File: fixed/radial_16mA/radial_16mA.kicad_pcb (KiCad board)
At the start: 2 copper layers, 25.4 x 20 mm, 18 parts, among them J1 Conn_01x04, J2 Conn_01x04, M1 MountingHole_2.5mm_Pad, M2 MountingHole_2.5mm_Pad, M3 MountingHole_2.5mm_Pad, M4 MountingHole_2.5mm_Pad, Q1 MMBT5551L, U1 TPS61222DCK, U2 LMV321

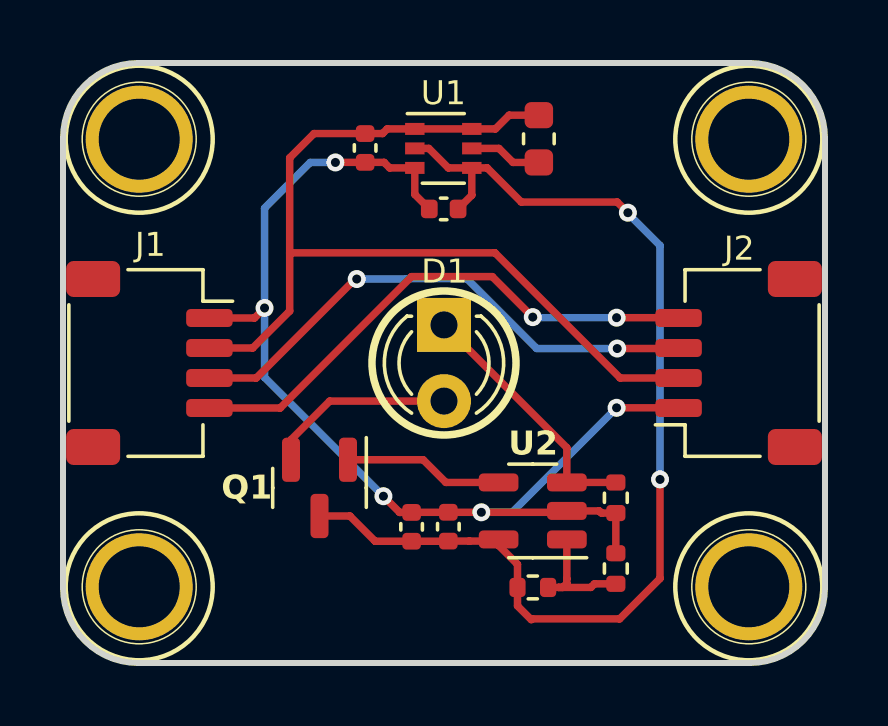
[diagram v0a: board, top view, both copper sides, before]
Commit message: Remade gerbers for fixed, radial 16mA and 24mA. Simplified traces slighly.
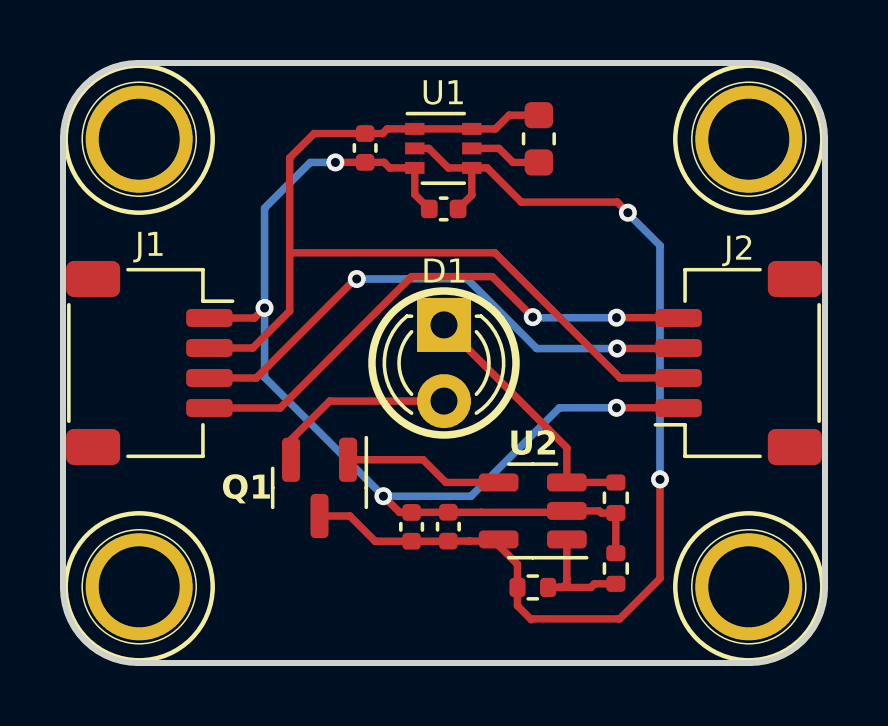
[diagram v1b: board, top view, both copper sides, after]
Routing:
- net GND: track 37.8 -> 40.8 mm, vias 5 -> 4
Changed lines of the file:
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@@
   (via (at 60.6806 64.4398) (size 0.6) (drill 0.3) (layers "F.Cu" "B.Cu") (net 1))
   (via (at 56.7182 58.166) (size 0.6) (drill 0.3) (layers "F.Cu" "B.Cu") (net 1))
-  (via (at 63.9452 64.976) (size 0.6) (drill 0.3) (layers "F.Cu" "B.Cu") (net 1))
   (via (at 59.0804 53.3146) (size 0.6) (drill 0.3) (layers "F.Cu" "B.Cu") (net 1))
   (via (at 68.453 61.4934) (size 0.6) (drill 0.3) (layers "F.Cu" "B.Cu") (net 1))
-  (segment (start 63.9452 64.976) (end 64.9704 64.976) (width 0.25) (layer "B.Cu") (net 1))
   (segment (start 56.7182 54.8386) (end 58.2422 53.3146) (width 0.25) (layer "B.Cu") (net 1))
-  (segment (start 63.915 64.9458) (end 63.9452 64.976) (width 0.25) (layer "B.Cu") (net 1))
+  (segment (start 60.6806 64.4398) (end 63.6016 64.4398) (width 0.25) (layer "B.Cu") (net 1))
+  (segment (start 63.6016 64.4398) (end 66.548 61.4934) (width 0.25) (layer "B.Cu") (net 1))
   (segment (start 56.7182 60.4774) (end 60.6806 64.4398) (width 0.25) (layer "B.Cu") (net 1))
   (segment (start 58.2422 53.3146) (end 59.0804 53.3146) (width 0.25) (layer "B.Cu") (net 1))
-  (segment (start 64.9704 64.976) (end 68.453 61.4934) (width 0.25) (layer "B.Cu") (net 1))
+  (segment (start 66.548 61.4934) (end 68.453 61.4934) (width 0.25) (layer "B.Cu") (net 1))
   (segment (start 56.7182 58.166) (end 56.7182 54.8386) (width 0.25) (layer "B.Cu") (net 1))
   (segment (start 56.7182 58.166) (end 56.7182 60.4774) (width 0.25) (layer "B.Cu") (net 1))
